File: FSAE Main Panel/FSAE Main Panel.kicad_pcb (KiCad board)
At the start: 2 copper layers, 244 parts, among them J1 Conn_01x08, J2 Conn_01x08, J3 Conn_01x10, J4 USB Micro B, J5 Cortex_Debug, J6 Conn_01x08, Q301 IRLML6402TRPBF, Q501 SI2308CDS-T1-GE3, Q502 SI2308CDS-T1-GE3, Q503 SI2308CDS-T1-GE3, Q504 SI2308CDS-T1-GE3, SW1 SW_SPST, SW2 SW_SPST, U101 SAMD21G18A-AU, U201 CD40106BPWR, U202 CD74HC238PWR, U301 TPS564201, U302 LM2940IMP-5.0/NOPB, U303 LP5907MFX-3.3, U304 LP5907MFX-3.3, U305 LP5907MFX-3.3, U401 MCP25625, U501 TLC6C598, U502 TLC6C5816, U503 TLC6C5816, Y101 32.768kHz, Y102 16MHz, Y401 16MHz

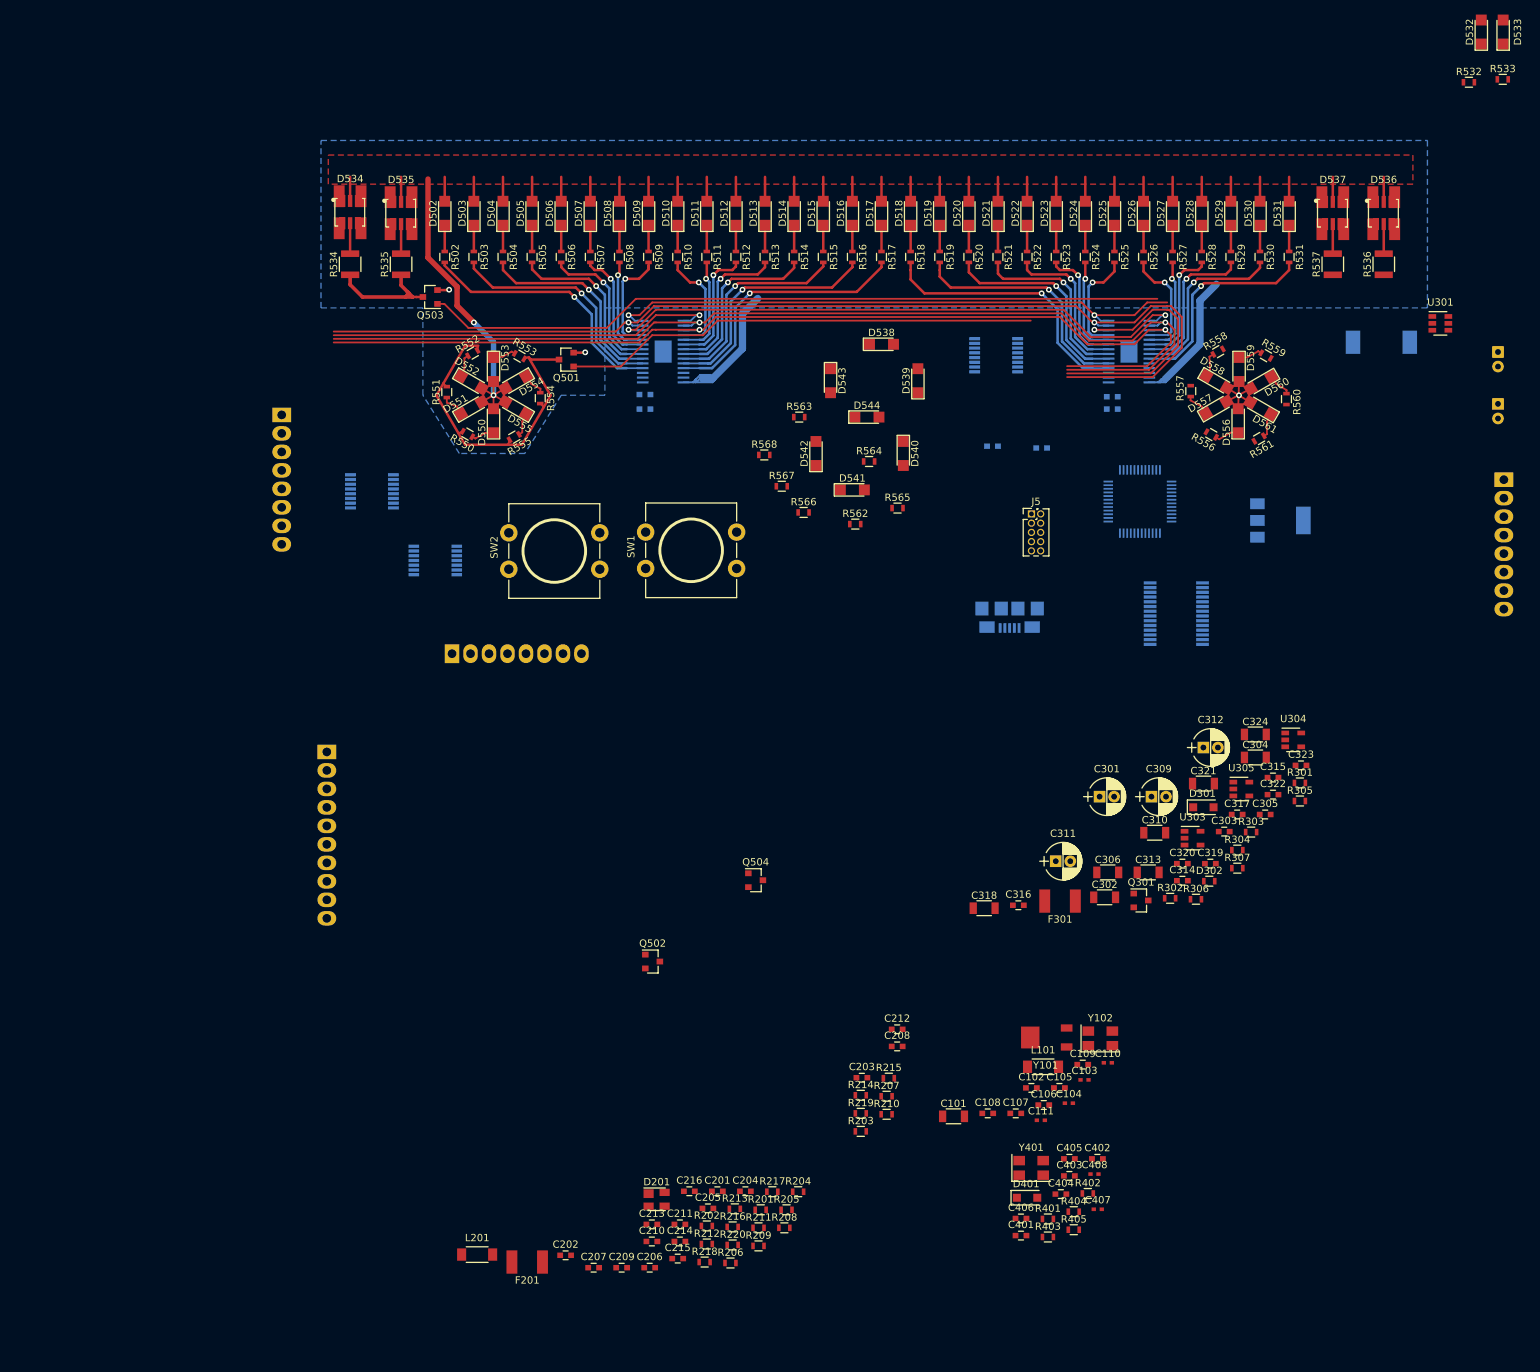
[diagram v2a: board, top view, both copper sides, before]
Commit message: Power Supply Layout
Finished 5V power supply.
Positioned DWC and Input Connectors
Completed CAL connector
Completed Clear Switch
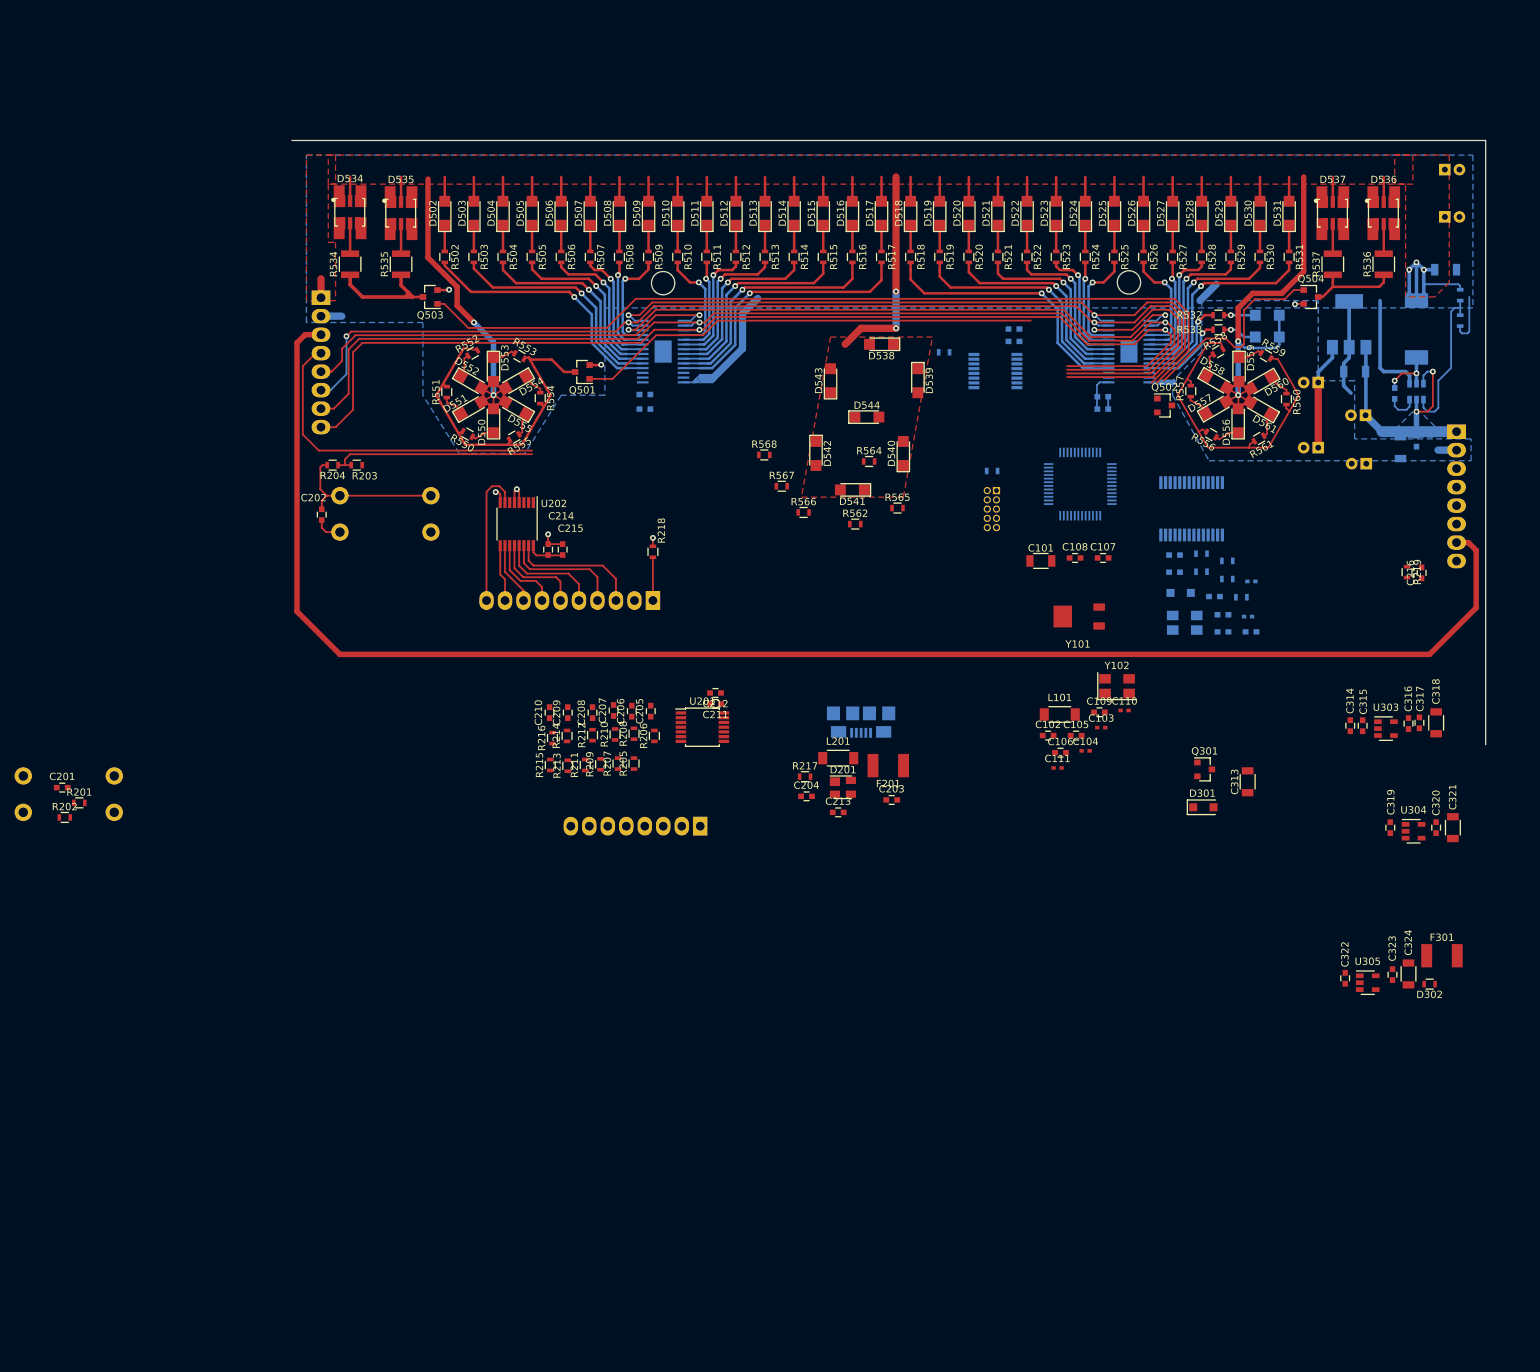
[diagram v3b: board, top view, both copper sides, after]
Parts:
- removed C304: 2.2uF, Capacitors_SMD:C_1206
- removed R303: 1k, Resistors_SMD:R_0603
- removed R304: 301k, Resistors_SMD:R_0603
- removed R305: 100k, Resistors_SMD:R_0603
- removed R306: 86.6k, Resistors_SMD:R_0603
- removed R307: 11.8k, Resistors_SMD:R_0603
- added REF**: MountingHole_3.2mm_M3, Mounting_Holes:MountingHole_3.2mm_M3, B.Cu at (219.0, 78.4)
- added REF**: MountingHole_3.2mm_M3, Mounting_Holes:MountingHole_3.2mm_M3, B.Cu at (155.0, 78.5)
- ALARM CLEAR: renamed from SW2; moved to B.Cu
- C301, C302, C303, C305, C306, C309, C310, C311, C312, C401, C402, C403, C404, C405, C406, C407, C408, D401, D532, D533, J5, R220, R301, R302, R401, R402, R403, R404, R405, R563, SW1, U301, Y401: moved to B.Cu
- U201, U202: moved to F.Cu
- moved C216 131.7 mm to (259.2, 118.4), turned to 90 degrees
- moved R204 118.5 mm to (109.6, 103.6), turned to 180 degrees
- moved R203 114.8 mm to (112.9, 103.6), turned to 180 degrees
- moved R220 112.1 mm to (200.2, 104.4), turned to 180 degrees
- moved Q504 110.6 mm to (244.0, 80.5)
- moved R201 109.0 mm to (74.8, 150.0)
- moved C202 107.1 mm to (108.1, 110.4), turned to 270 degrees
- moved C201 105.7 mm to (72.5, 147.9)
- moved R219 105.6 mm to (257.2, 118.3), turned to 270 degrees
- moved R202 104.5 mm to (72.8, 152.0)
- moved Q502 103.9 mm to (223.9, 95.4)
- moved C215 98.7 mm to (141.2, 115.2), turned to 90 degrees
- moved R218 97.8 mm to (153.6, 115.5), turned to 90 degrees
- moved C214 96.8 mm to (139.2, 115.2), turned to 90 degrees
- moved R403 96.2 mm to (229.0, 115.8)
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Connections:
- J3 pad 2: /External Interface/CAL1 -> GND
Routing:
- net ~NEUT: track 0.00 -> 218.8 mm
- net LED_+5V: track 170.0 -> 272.0 mm, vias 3 -> 9
- net /Display/OP_CONTROL: track 0.00 -> 46.9 mm
- net DWC_CONT: track 0.00 -> 45.0 mm
- net GND: track 48.6 -> 91.2 mm, vias 2 -> 7
- net CAN_V+: track 0.00 -> 37.1 mm, vias 0 -> 2
- net ~CLEAR: track 0.00 -> 28.6 mm
- net SHIFT2: track 0.00 -> 28.1 mm
- net /External Interface/SW2_L: track 0.00 -> 21.8 mm
- net Net-(R301-Pad2): track 0.00 -> 21.0 mm
- net /External Interface/CAL9: track 0.00 -> 19.6 mm
- net /External Interface/CAL2: track 0.00 -> 18.1 mm
- net SHIFT1: track 101.9 -> 118.6 mm
- net /External Interface/CAL3: track 0.00 -> 16.5 mm
- net +5V: track 0.00 -> 14.6 mm
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- added copper zone on B.Cu, net CAN_V+
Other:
- board outline added: 164 x 83 mm

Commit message: Complete External IO
All Connectors placed and wired
Buttons placed and wired
External 3.3V regulator complete
Cal Input IC Complete
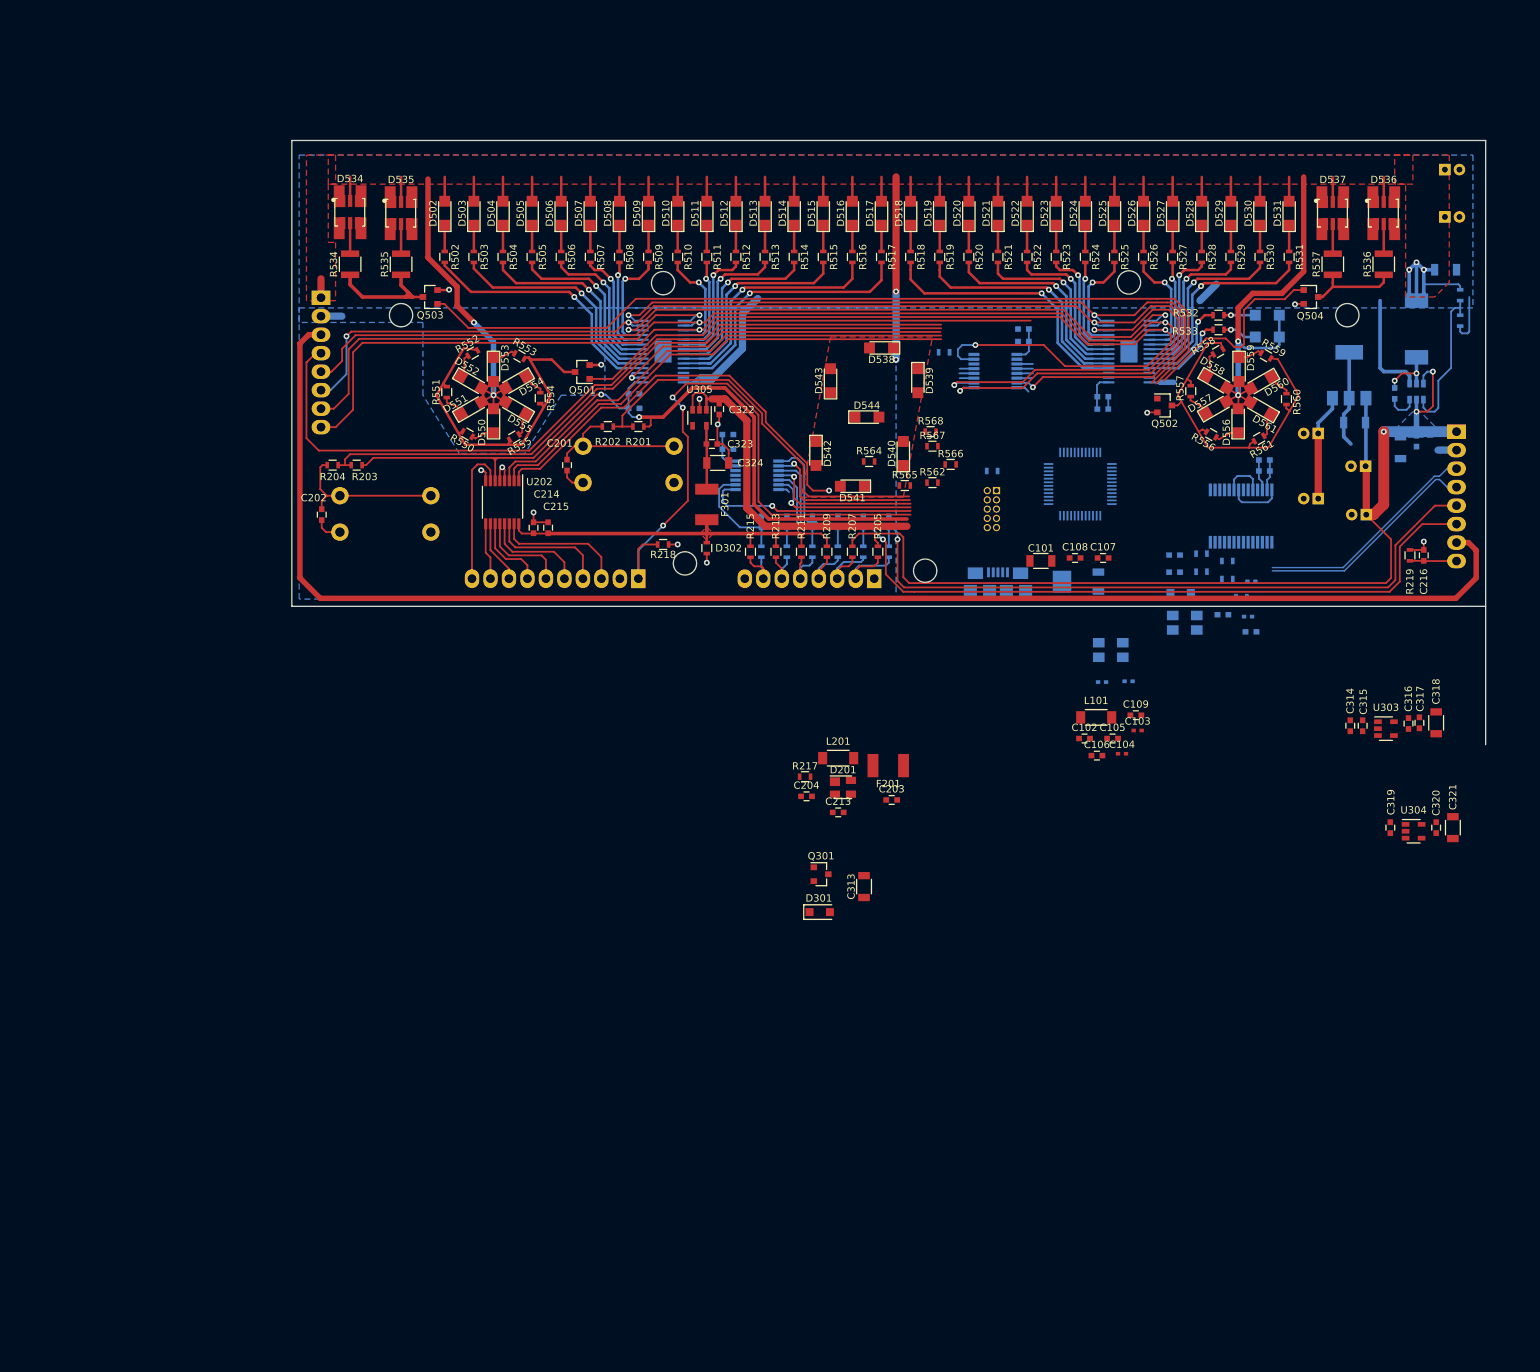
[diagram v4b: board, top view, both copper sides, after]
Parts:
- added REF**: MountingHole_3.2mm_M3, Mounting_Holes:MountingHole_3.2mm_M3, B.Cu at (158.0, 117.0)
- added REF**: MountingHole_3.2mm_M3, Mounting_Holes:MountingHole_3.2mm_M3, B.Cu at (191.0, 118.0)
- added REF**: MountingHole_3.2mm_M3, Mounting_Holes:MountingHole_3.2mm_M3, B.Cu at (249.0, 82.9)
- added REF**: MountingHole_3.2mm_M3, Mounting_Holes:MountingHole_3.2mm_M3, B.Cu at (119.0, 82.9)
- C110, C111, C205, C206, C207, C208, C209, C210, C211, C212, R206, R208, R210, R212, R214, R216, U201, Y101, Y102: moved to B.Cu
- moved U305 120.2 mm to (160.0, 97.1), turned to 270 degrees
- moved C323 118.6 mm to (161.7, 100.7), turned to 0 degrees
- moved F301 118.5 mm to (161.0, 109.0), turned to 90 degrees
- moved C324 118.0 mm to (162.5, 103.3), turned to 0 degrees
- moved C322 116.2 mm to (162.7, 95.9)
- moved D302 116.0 mm to (161.0, 115.0), turned to 270 degrees
- moved R201 92.6 mm to (151.6, 98.3), turned to 180 degrees
- moved R202 91.9 mm to (147.4, 98.3), turned to 180 degrees
- moved RESET 89.3 mm to (144.0, 106.0)
- moved C201 82.3 mm to (141.8, 103.6), turned to 270 degrees
- moved C313 54.6 mm to (182.6, 161.5)
- moved Q301 54.6 mm to (176.7, 159.8)
- moved D301 54.6 mm to (176.5, 165.0)
- moved R205 44.4 mm to (184.5, 115.5)
- moved R207 43.4 mm to (181.0, 115.5)
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- renumbered SW1 to RESET
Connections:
- U401 pad 27: (no net) -> +5V
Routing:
- net +3V3: track 5.06 -> 124.7 mm, vias 0 -> 2
- net CAN_V+: track 37.1 -> 147.0 mm, vias 2 -> 3
- net DSFT: track 0.00 -> 97.0 mm, vias 0 -> 1
- net USFT: track 0.00 -> 95.4 mm, vias 0 -> 1
- net CAL_IN: track 5.95 -> 83.5 mm, vias 0 -> 3
- net CAL_c: track 0.00 -> 68.7 mm
- net CAL_b: track 0.00 -> 67.7 mm
- net ~CLEAR: track 28.6 -> 92.0 mm
- net DWC_CONT: track 45.0 -> 108.0 mm
- net CAL_a: track 0.00 -> 58.4 mm, vias 0 -> 1
- net ~RESET: track 0.00 -> 55.2 mm
- net EXT_+3V3: track 5.23 -> 55.1 mm
- net ~PWM_GREEN: track 0.00 -> 48.6 mm, vias 0 -> 1
- net /Power/+5V_INT: track 0.00 -> 47.9 mm
- net CAN_IN-: track 0.00 -> 30.9 mm
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- added copper zone on F.Cu, net EXT_+3V3
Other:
- outline, holes or cut-outs redrawn
- board text added: "5V"
- board text added: "C1"
- board text added: "C2"
- board text added: "C3"
- board text added: "C4"
- board text added: "C5"
- board text added: "C6"
- board text added: "C7"
- board text added: "C8"
- board text added: "C9"
- board text added: "CAL"
- board text added: "CLK"
- board text added: "CLR"
- board text added: "CON"
- board text added: "FRAME"
- board text added: "GND"
- board text added: "NEUT"
- board text added: "SET"
